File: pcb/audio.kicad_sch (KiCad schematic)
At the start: 24 parts, among them J5 Conn_01x03, J6 SJ2-3593D-SMT-TR, U17 PCM5102A, U18 PC817C-S

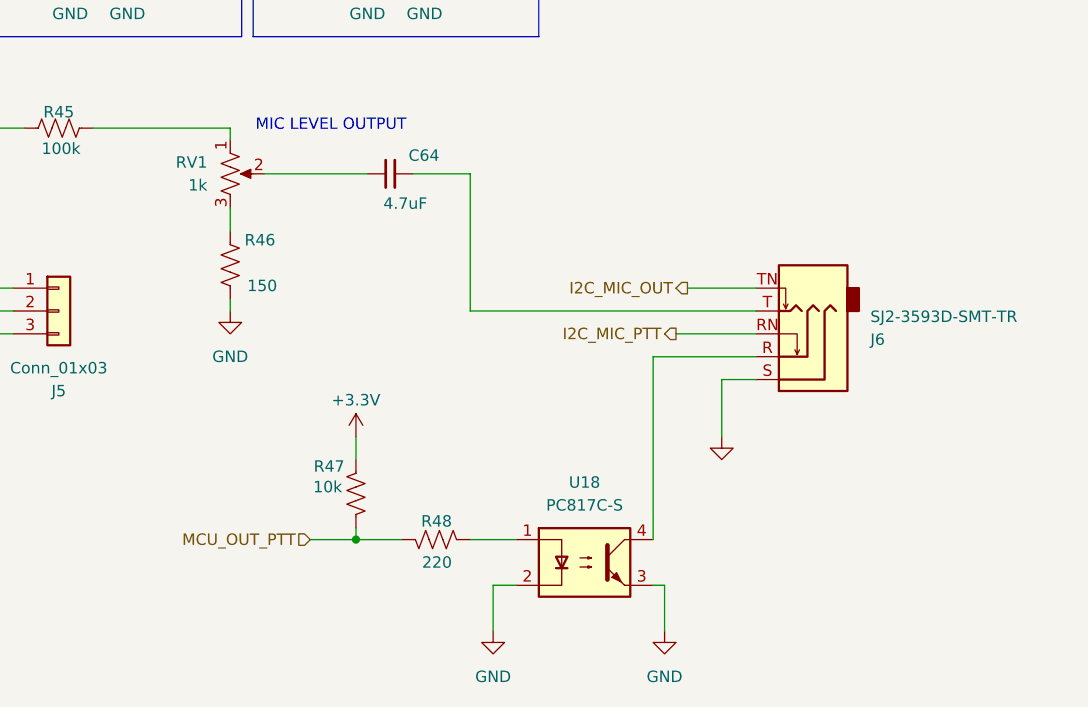
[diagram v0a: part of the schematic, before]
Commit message: Move audio jack (J6) into SA818V sheet, rename nets/jumpers for clarity
Relocates the switched TRS jack from audio.kicad_sch into SA818V.kicad_sch
and updates the root sheet's pin interface to match (SA818_IN_MIC,
SA818_IN_PTT, new SA818_IN_PTT_HB), fixing an I2C_MIC_OUT/I2S_MIC_OUT
naming typo along the way. Ring/ring-switch/sleeve are wired; tip and
tip-switch (mic audio leg) are still open, per audio_ptt_path.md.

Also: renames GPS hierarchical labels and several power/regulation/
peripheral jumper values from generic (Jumper_2_Open, SolderJumper_2_Open)
to descriptive names, wires MCU_OUT_PTT_HB, and removes now-unused test
points/jumpers from the battery input sheets. Adds 74hc123_pinout.md
planning doc for the TX-safety timeout / force-off failsafe part.

Co-Authored-By: Claude Sonnet 5 <noreply@anthropic.com>
Claude-Session: https://claude.ai/code/session_01P3G1ionr2QCR8SZtKRreL3
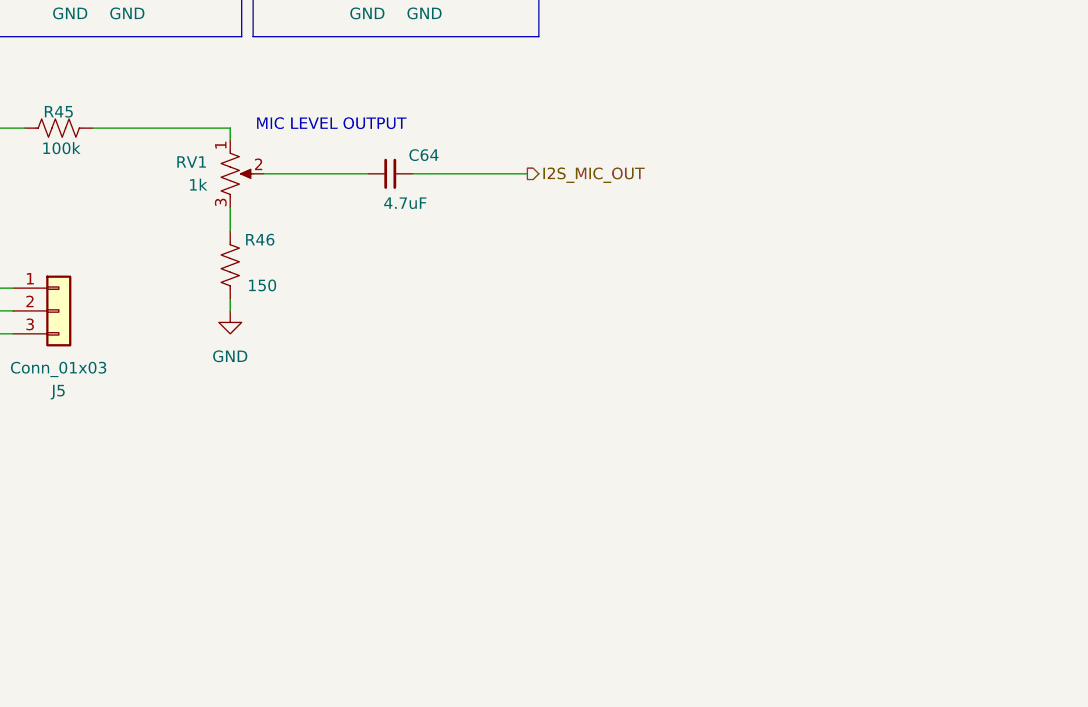
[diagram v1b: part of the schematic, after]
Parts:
- removed J6: SJ2-3593D-SMT-TR, Connector_Audio:Jack_3.5mm_CUI_SJ2-3593D-SMT_Horizontal, symbol Connector_Audio:AudioJack3_SwitchTR
- removed R47: 10k, Resistor_SMD:R_0603_1608Metric, symbol Device:R_US
- removed R48: 220, Resistor_SMD:R_0603_1608Metric, symbol Device:R_US
- removed U18: PC817C-S, Package_SO:SOP-4_7.5x4.1mm_P2.54mm, symbol Isolator:PC817
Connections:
- net I2S_MIC_OUT: now reaches C64.1
